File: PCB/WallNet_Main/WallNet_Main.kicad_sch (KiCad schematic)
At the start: 15 parts, among them J1 Conn_01x05_Pin, SW1 SW, U1 BT832

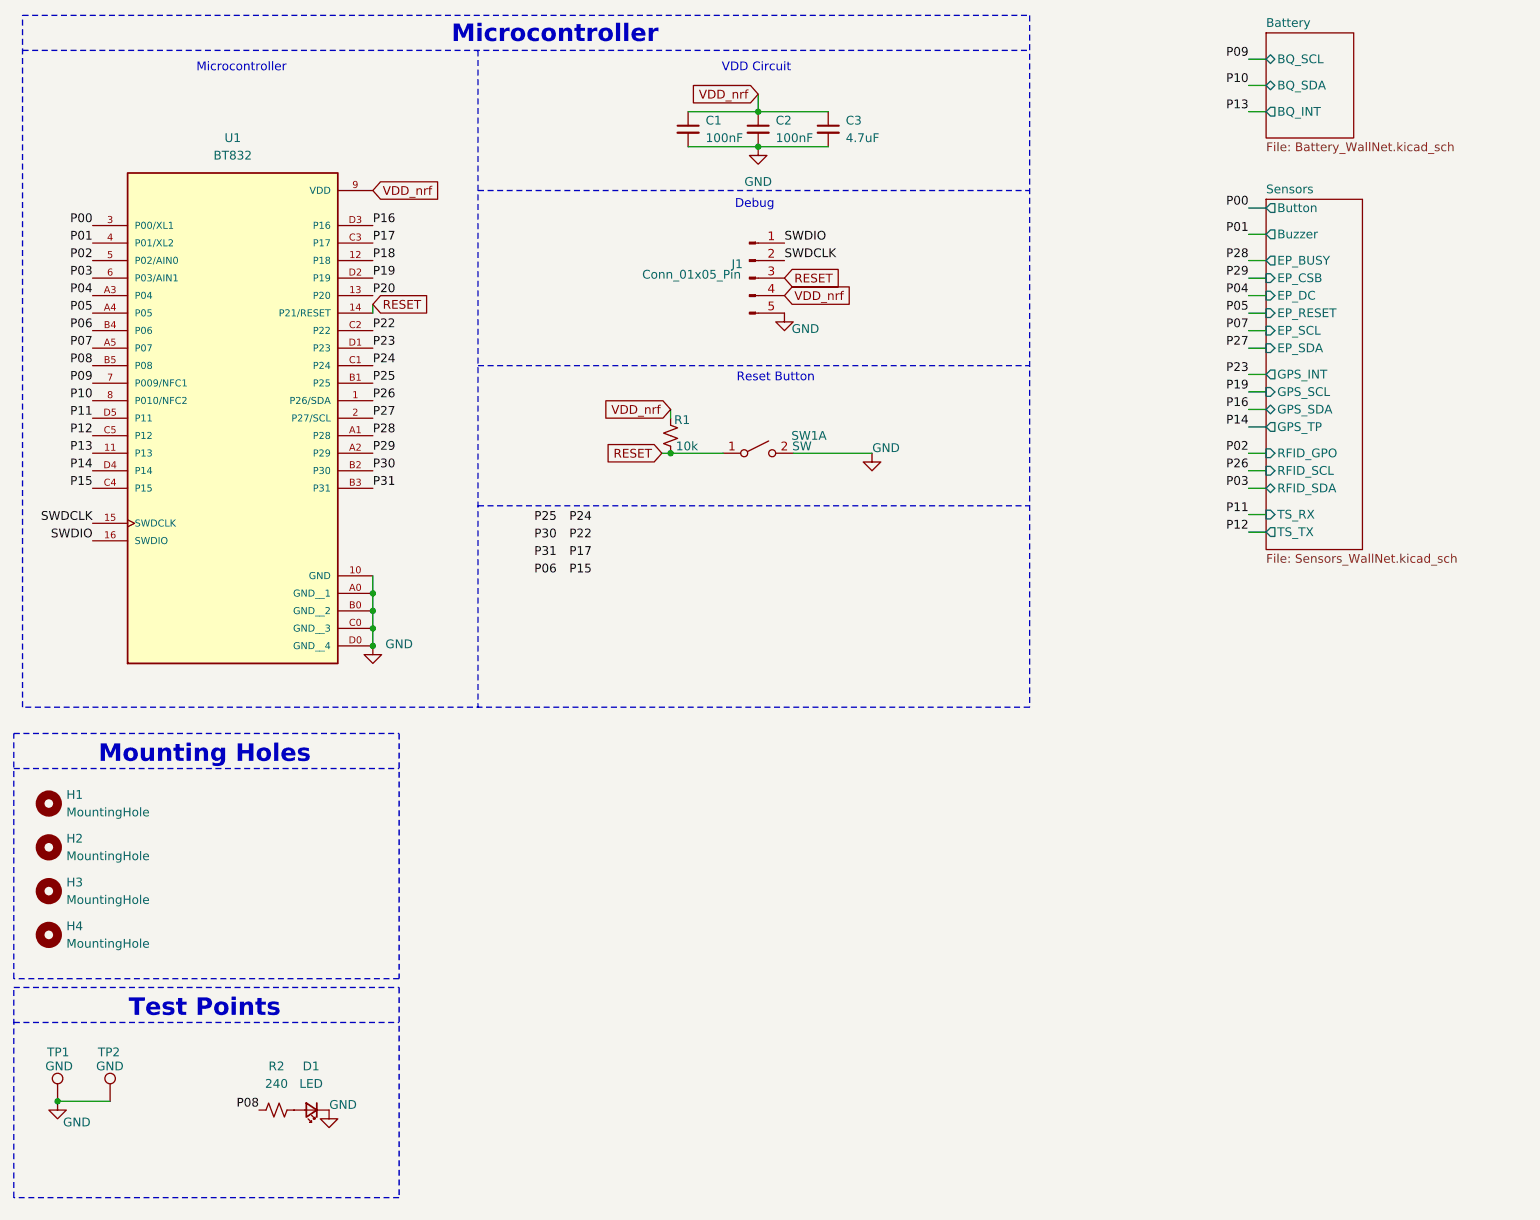
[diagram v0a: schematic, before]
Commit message: Redid PCB still need to DRC the design
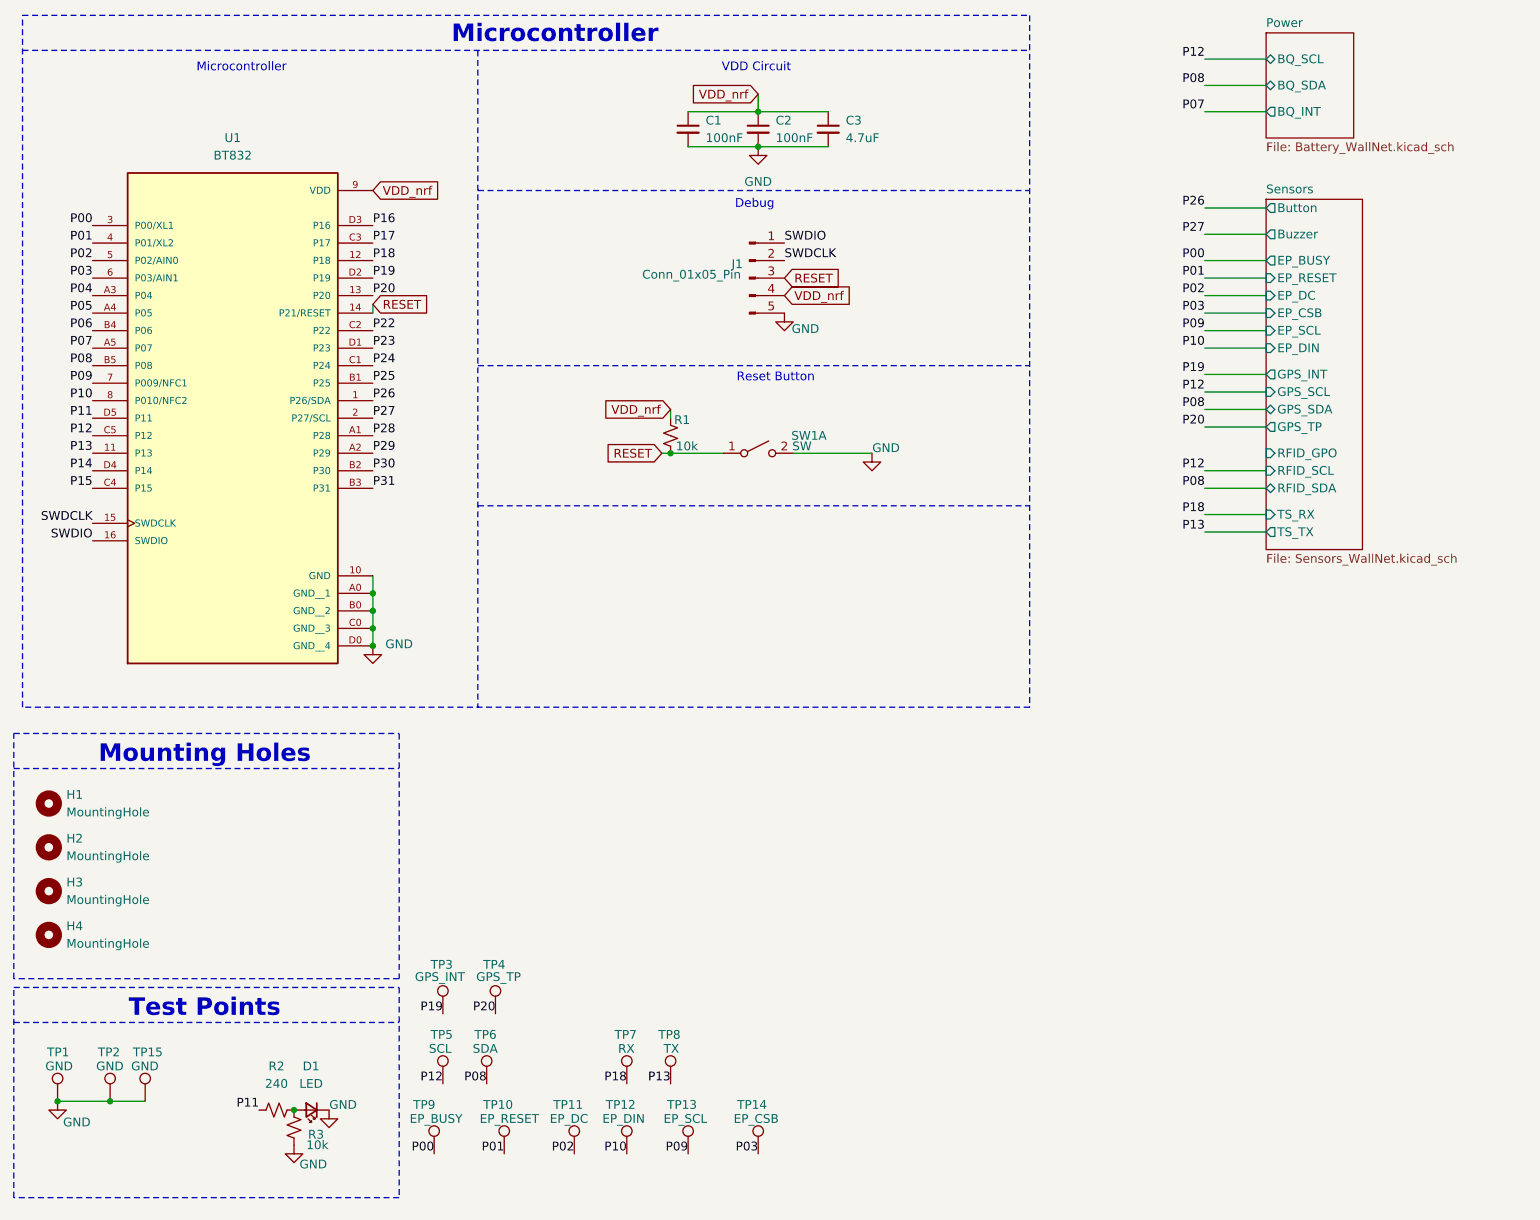
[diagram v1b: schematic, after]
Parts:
- added R3: 10k, Resistor_SMD:R_0603_1608Metric, symbol Device:R_Small_US
- added TP10: EP_RESET, 5001:KEYSTONE_5001, symbol Connector:TestPoint
- added TP11: EP_DC, 5001:KEYSTONE_5001, symbol Connector:TestPoint
- added TP12: EP_DIN, 5001:KEYSTONE_5001, symbol Connector:TestPoint
- added TP13: EP_SCL, 5001:KEYSTONE_5001, symbol Connector:TestPoint
- added TP14: EP_CSB, 5001:KEYSTONE_5001, symbol Connector:TestPoint
- added TP15: GND, 5001:KEYSTONE_5001, symbol Connector:TestPoint
- added TP3: GPS_INT, 5001:KEYSTONE_5001, symbol Connector:TestPoint
- added TP4: GPS_TP, 5001:KEYSTONE_5001, symbol Connector:TestPoint
- added TP5: SCL, 5001:KEYSTONE_5001, symbol Connector:TestPoint
- added TP6: SDA, 5001:KEYSTONE_5001, symbol Connector:TestPoint
- added TP7: RX, 5001:KEYSTONE_5001, symbol Connector:TestPoint
- added TP8: TX, 5001:KEYSTONE_5001, symbol Connector:TestPoint
- added TP9: EP_BUSY, 5001:KEYSTONE_5001, symbol Connector:TestPoint
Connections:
- net GND: now also R3.1, TP15.1
- net P00: now also TP9.1
- net P01: now also TP10.1
- net P02: now also TP11.1
- net P03: now also TP14.1
- net P08: now also TP6.1; no longer R2.1
- net P09: now also TP13.1
- net P10: now also TP12.1
- net P11: now also R2.1
- net P12: now also TP5.1
- net P13: now also TP8.1
- net P18: now also TP7.1
- net P19: now also TP3.1
- net P20: now also TP4.1
- net at D1.2 (A), R2.2: now also R3.2
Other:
- sheet Battery renamed Power
- sheet Sensors ports: added EP_DIN; removed EP_SDA

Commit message: Implemented most changes
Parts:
- added D2: LED, Diode_SMD:D_0603_1608Metric, symbol Device:LED_Small
- added R4: 240, Resistor_SMD:R_0603_1608Metric, symbol Device:R_Small_US
- added R5: 10k, Resistor_SMD:R_0603_1608Metric, symbol Device:R_Small_US
- added TP16, TP17, TP18, TP19: Pad, TestPoint:TestPoint_Pad_1.0x1.0mm, symbol Connector:TestPoint_Alt
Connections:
- net GND: now also D2.1 (K), R5.1
- net P04: now also TP18.1
- net P05: now also TP19.1
- net P14: now also R4.1
- net P28: now also TP16.1
- net P29: now also TP17.1
- new net: D2.2 (A), R4.2, R5.2
- no-connect marks 0 -> 10
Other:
- note added: "Pads"
- moved on the sheet: D1, H2, H3, H4, R2, R3, TP1, TP10, TP11, TP12, TP13, TP14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
